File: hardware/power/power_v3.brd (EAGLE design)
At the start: 92 x 92 mm, 53 parts, among them J1 LINEAR_2_5040500291, J10 LINEAR_2_5040500291, J2 PWR_2_XT30PW-F, J3 PWR_2_XT30PW-F, J4 PWR_2_XT30PW-F, J5 PWR_2_XT30PW-F, J6 FASTON, J7 FASTON, J8 PWR_4, J9 PWR_4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

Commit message: Moving mounting holes around
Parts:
- moved D5 4.72 mm to (39.5, 5.70)
- moved C14 4.72 mm to (37.2, 5.70)
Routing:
- net N$21: track 41.7 -> 40.1 mm
- net -V_BATT: vias 22 -> 19
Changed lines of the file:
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@@
 <layer number="43" name="vRestrict" color="2" fill="10" visible="yes" active="yes"/>
 <layer number="44" name="Drills" color="7" fill="1" visible="no" active="yes"/>
-<layer number="45" name="Holes" color="7" fill="1" visible="no" active="yes"/>
+<layer number="45" name="Holes" color="7" fill="1" visible="yes" active="yes"/>
 <layer number="46" name="Milling" color="3" fill="1" visible="no" active="yes"/>
 <layer number="47" name="Measures" color="7" fill="1" visible="no" active="yes"/>
@@
 <circle x="46" y="3" radius="3" width="0.2" layer="21"/>
 <circle x="3" y="3" radius="3" width="0.2" layer="21"/>
+<hole x="3" y="89" drill="3.4"/>
+<hole x="46" y="89" drill="3.4"/>
+<hole x="89" y="89" drill="3.4"/>
+<hole x="89" y="3" drill="3.4"/>
+<hole x="46" y="3" drill="3.4"/>
+<hole x="3" y="3" drill="3.4"/>
 </plain>
 <attributes>
@@
 <attribute name="VALUE" x="11.03" y="20.36" size="1.27" layer="27"/>
 </element>
-<element name="C14" library="_T_rcl" library_urn="urn:adsk.eagle:library:19571919" package="C0603" package3d_urn="urn:adsk.eagle:package:19572011/3" value="0.068uF 50V" x="41.9" y="6.1" smashed="yes" rot="R90">
-<attribute name="NAME" x="40.63" y="4.83" size="1.27" layer="25" rot="R90"/>
-<attribute name="VALUE" x="44.44" y="4.83" size="1.27" layer="27" rot="R90"/>
-</element>
-<element name="D5" library="_T_rcl" library_urn="urn:adsk.eagle:library:19571919" package="SOD123" package3d_urn="urn:adsk.eagle:package:20295471/2" value="5_0SMDJ24A" x="44.2" y="6.1" smashed="yes" rot="R270">
-<attribute name="NAME" x="45.2" y="8.1" size="1.27" layer="25" rot="R270"/>
-<attribute name="VALUE" x="41.7" y="8.1" size="1.27" layer="27" rot="R270"/>
+<element name="C14" library="_T_rcl" library_urn="urn:adsk.eagle:library:19571919" package="C0603" package3d_urn="urn:adsk.eagle:package:19572011/3" value="0.068uF 50V" x="37.2" y="5.7" smashed="yes" rot="R90">
+<attribute name="NAME" x="35.93" y="4.43" size="1.27" layer="25" rot="R90"/>
+<attribute name="VALUE" x="39.74" y="4.43" size="1.27" layer="27" rot="R90"/>
+</element>
+<element name="D5" library="_T_rcl" library_urn="urn:adsk.eagle:library:19571919" package="SOD123" package3d_urn="urn:adsk.eagle:package:20295471/2" value="5_0SMDJ24A" x="39.5" y="5.7" smashed="yes" rot="R270">
+<attribute name="NAME" x="40.5" y="7.7" size="1.27" layer="25" rot="R270"/>
+<attribute name="VALUE" x="37" y="7.7" size="1.27" layer="27" rot="R270"/>
 </element>
 </elements>
@@
 <wire x1="23" y1="13.9" x2="23.1" y2="13.8" width="0.2" layer="1"/>
 <via x="23.1" y="13.8" extent="1-16" drill="0.29"/>
-<wire x1="23.1" y1="13.8" x2="34.1" y2="2.8" width="0.2" layer="16"/>
-<wire x1="34.1" y1="2.8" x2="50.6" y2="2.8" width="0.2" layer="16"/>
+<wire x1="23.1" y1="13.8" x2="28.2" y2="8.7" width="0.2" layer="16"/>
+<wire x1="44.7" y1="8.7" x2="28.2" y2="8.7" width="0.2" layer="16"/>
+<wire x1="44.7" y1="8.7" x2="50.6" y2="2.8" width="0.2" layer="16"/>
 <via x="50.6" y="2.8" extent="1-16" drill="0.29"/>
 <polygon width="0.1524" layer="1" isolate="0.6" thermals="no">
@@
 <contactref element="C14" pad="1"/>
 <contactref element="D5" pad="C"/>
-<wire x1="41.9" y1="6.85" x2="41.9" y2="7.8" width="1" layer="1"/>
-<via x="41.9" y="7.8" extent="1-16" drill="0.75"/>
-<wire x1="44.2" y1="7.675" x2="44.075" y2="7.8" width="0.2" layer="1"/>
-<wire x1="44.075" y1="7.8" x2="41.9" y2="7.8" width="1" layer="1"/>
+<wire x1="37.2" y1="6.45" x2="37.2" y2="7.4" width="1" layer="1"/>
+<via x="37.2" y="7.4" extent="1-16" drill="0.75"/>
+<wire x1="39.5" y1="7.275" x2="39.375" y2="7.4" width="0.2" layer="1"/>
+<wire x1="39.375" y1="7.4" x2="37.2" y2="7.4" width="1" layer="1"/>
 <polygon width="0.2" layer="1" isolate="0.3" thermals="no">
 <vertex x="20.1" y="26.6"/>
@@
 <contactref element="C14" pad="2"/>
 <contactref element="D5" pad="A"/>
-<wire x1="41.9" y1="5.35" x2="41.9" y2="4.5" width="1" layer="1"/>
-<via x="41.9" y="4.5" extent="1-16" drill="0.75"/>
-<wire x1="44.2" y1="4.525" x2="44.175" y2="4.5" width="0.2" layer="1"/>
-<wire x1="44.175" y1="4.5" x2="41.9" y2="4.5" width="1" layer="1"/>
-<via x="89" y="89" extent="1-16" drill="3"/>
-<via x="3" y="89" extent="1-16" drill="3"/>
-<via x="46" y="89" extent="1-16" drill="3"/>
+<wire x1="37.2" y1="4.95" x2="37.2" y2="4.1" width="1" layer="1"/>
+<via x="37.2" y="4.1" extent="1-16" drill="0.75"/>
+<wire x1="39.5" y1="4.125" x2="39.475" y2="4.1" width="0.2" layer="1"/>
+<wire x1="39.475" y1="4.1" x2="37.2" y2="4.1" width="1" layer="1"/>
 </signal>
 <signal name="N$10">
@@
 <via x="17.2" y="5.1" extent="1-16" drill="0.29"/>
 <wire x1="17.2" y1="5.1" x2="15" y2="2.9" width="0.2" layer="16"/>
-<wire x1="15" y1="2.9" x2="4" y2="2.9" width="0.2" layer="16"/>
-<wire x1="4" y1="2.9" x2="1.4" y2="5.5" width="0.2" layer="16"/>
+<wire x1="15" y1="2.9" x2="6.7" y2="2.9" width="0.2" layer="16"/>
+<wire x1="6.7" y1="2.9" x2="1.4" y2="8.2" width="0.2" layer="16"/>
 <wire x1="1.4" y1="24.3" x2="2.6" y2="25.5" width="0.2" layer="16"/>
 <via x="2.6" y="25.5" extent="1-16" drill="0.29"/>
 <wire x1="2.6" y1="25.5" x2="2.95" y2="25.85" width="0.2" layer="1"/>
 <wire x1="2.95" y1="25.85" x2="4.5" y2="25.85" width="0.2" layer="1"/>
-<wire x1="1.4" y1="5.5" x2="1.4" y2="24.3" width="0.2" layer="16"/>
+<wire x1="1.4" y1="8.2" x2="1.4" y2="24.3" width="0.2" layer="16"/>
 </signal>
 <signal name="N$22">
@@
 <wire x1="14.9" y1="58.81" x2="14.94" y2="58.85" width="0.2" layer="1"/>
 </signal>
-<signal name="-V_BATT1">
-<via x="89" y="3" extent="1-16" drill="3"/>
-<via x="3" y="3" extent="1-16" drill="3"/>
-<via x="46" y="3" extent="1-16" drill="3"/>
-<wire x1="46" y1="3" x2="89" y2="3" width="0" layer="19" extent="1-1"/>
-<wire x1="3" y1="3" x2="46" y2="3" width="0" layer="19" extent="1-1"/>
-</signal>
 </signals>

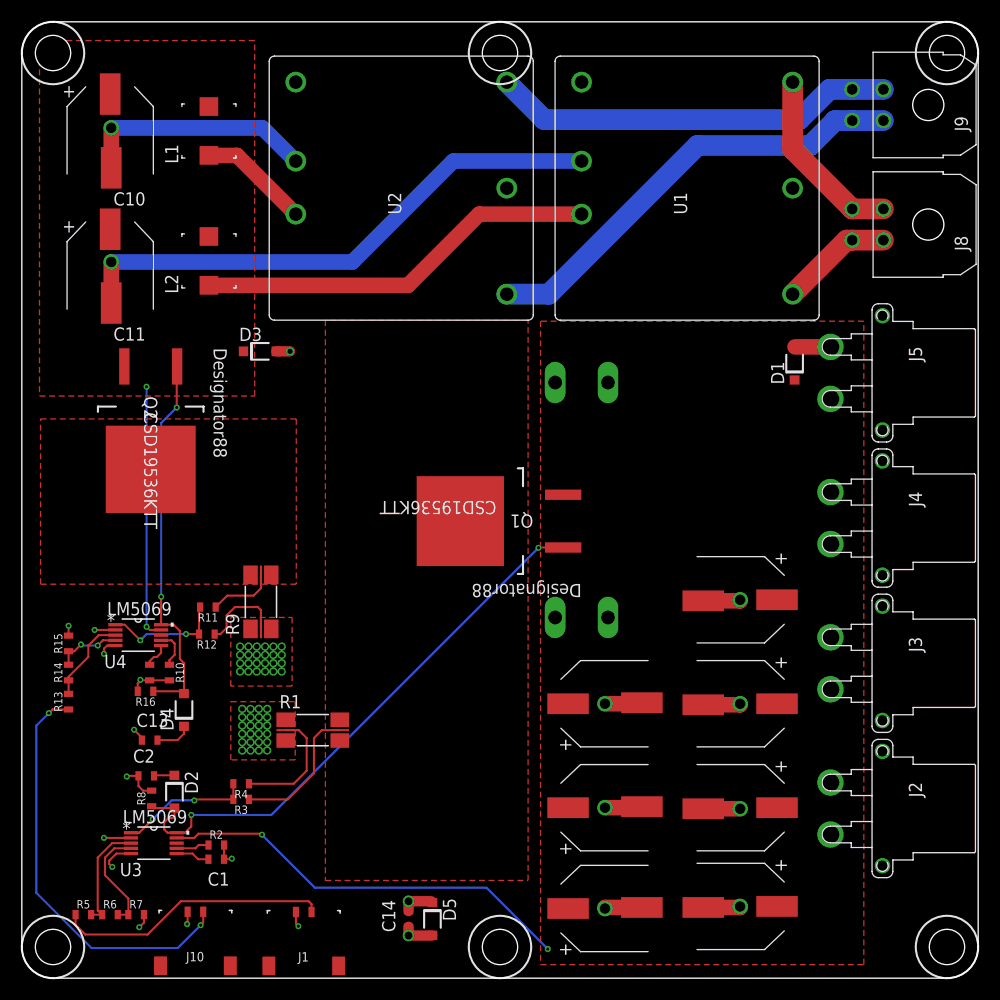
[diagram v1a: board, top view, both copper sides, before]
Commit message: Moved parts for mounting, now uploading
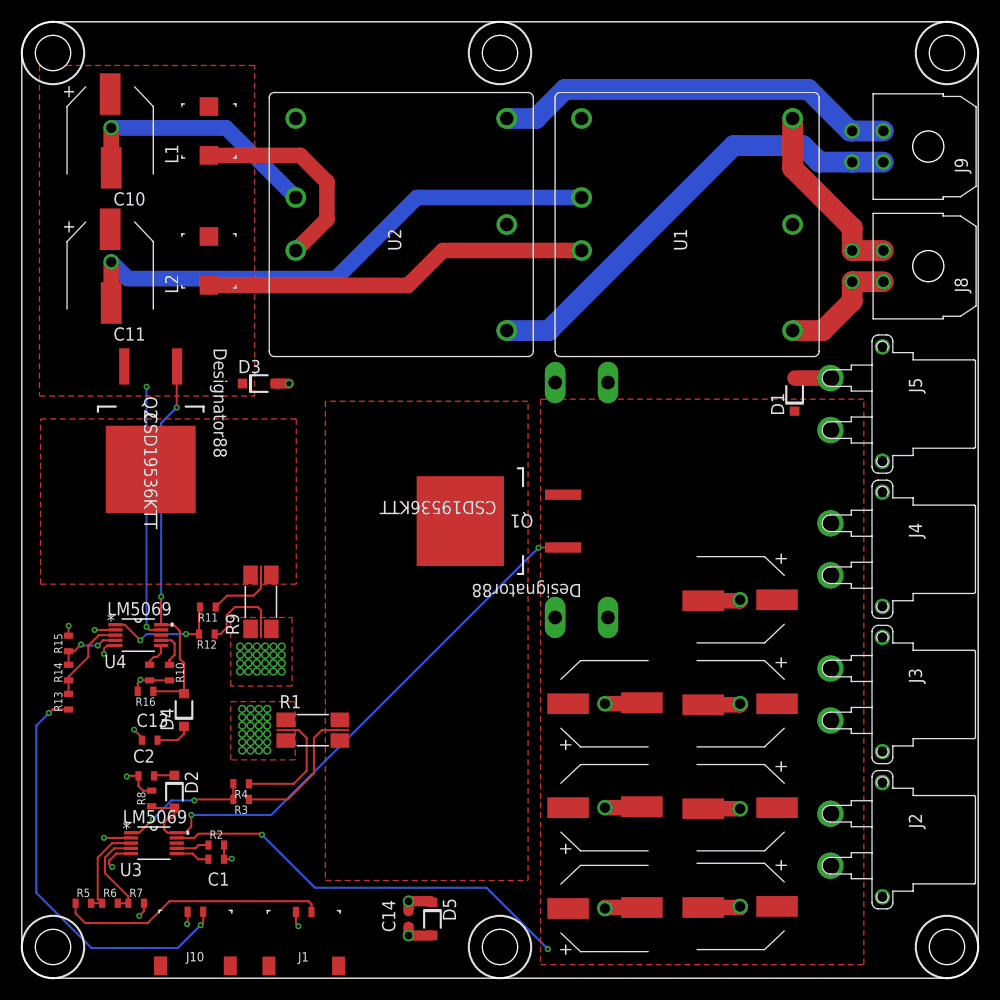
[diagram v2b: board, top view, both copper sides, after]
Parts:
- moved J8 4.00 mm to (87.2, 68.5)
- moved J9 4.00 mm to (87.2, 80.0)
- moved U1 3.50 mm to (64.0, 72.5)
- moved U2 3.50 mm to (36.5, 72.5)
- moved D3 3.10 mm to (22.8, 57.2)
- moved D1 3.00 mm to (74.3, 56.1)
- moved J2 3.00 mm to (82.8, 13.3)
- moved J3 3.00 mm to (82.8, 27.3)
- moved J4 3.00 mm to (82.8, 41.3)
- moved J5 3.00 mm to (82.8, 55.2)
- moved R5 1.10 mm to (5.92, 7.21)
- moved R6 1.10 mm to (8.48, 7.21)
- moved R7 1.10 mm to (11.0, 7.21)
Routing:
- net N$12: track 10.7 -> 20.2 mm
- net N$13: track 38.7 -> 37.2 mm
- net -V_BATT: track 127.7 -> 129.0 mm
- net +12V: track 43.1 -> 44.3 mm
- net N$8: track 10.5 -> 9.39 mm
- net N$9: track 10.3 -> 9.21 mm
- net +5V: track 10.9 -> 11.8 mm
- net 5V_GND: track 17.6 -> 18.1 mm
